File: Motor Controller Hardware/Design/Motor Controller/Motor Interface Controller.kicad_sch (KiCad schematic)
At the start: 0 parts

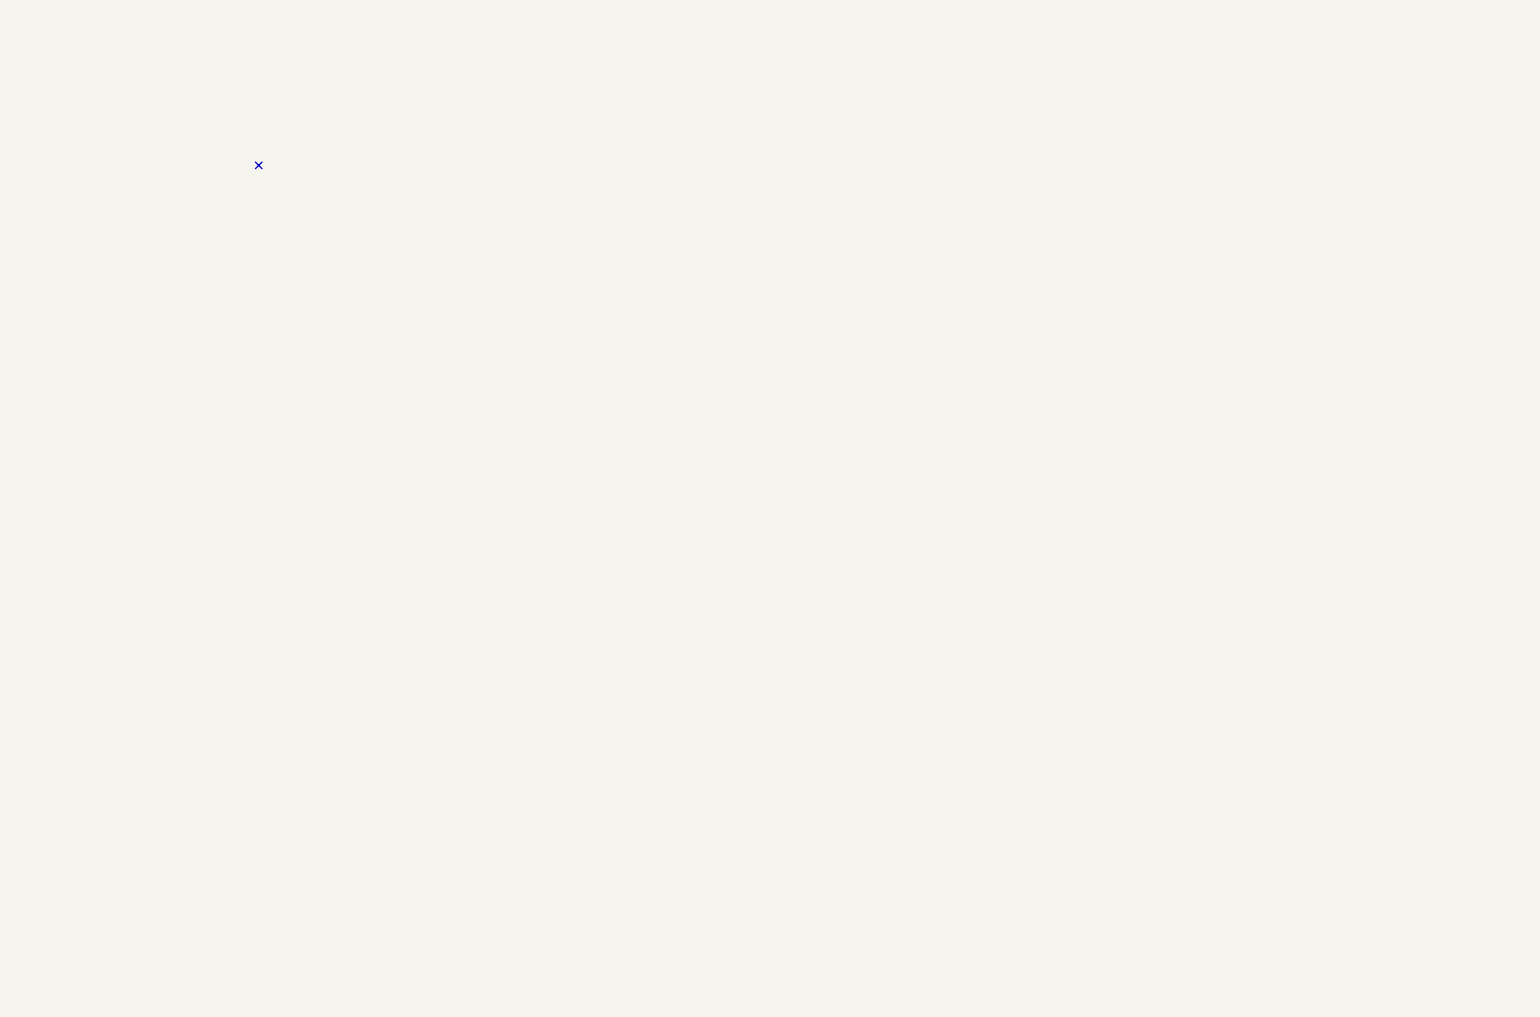
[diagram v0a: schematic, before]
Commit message: Made interface controller and finished gate drive
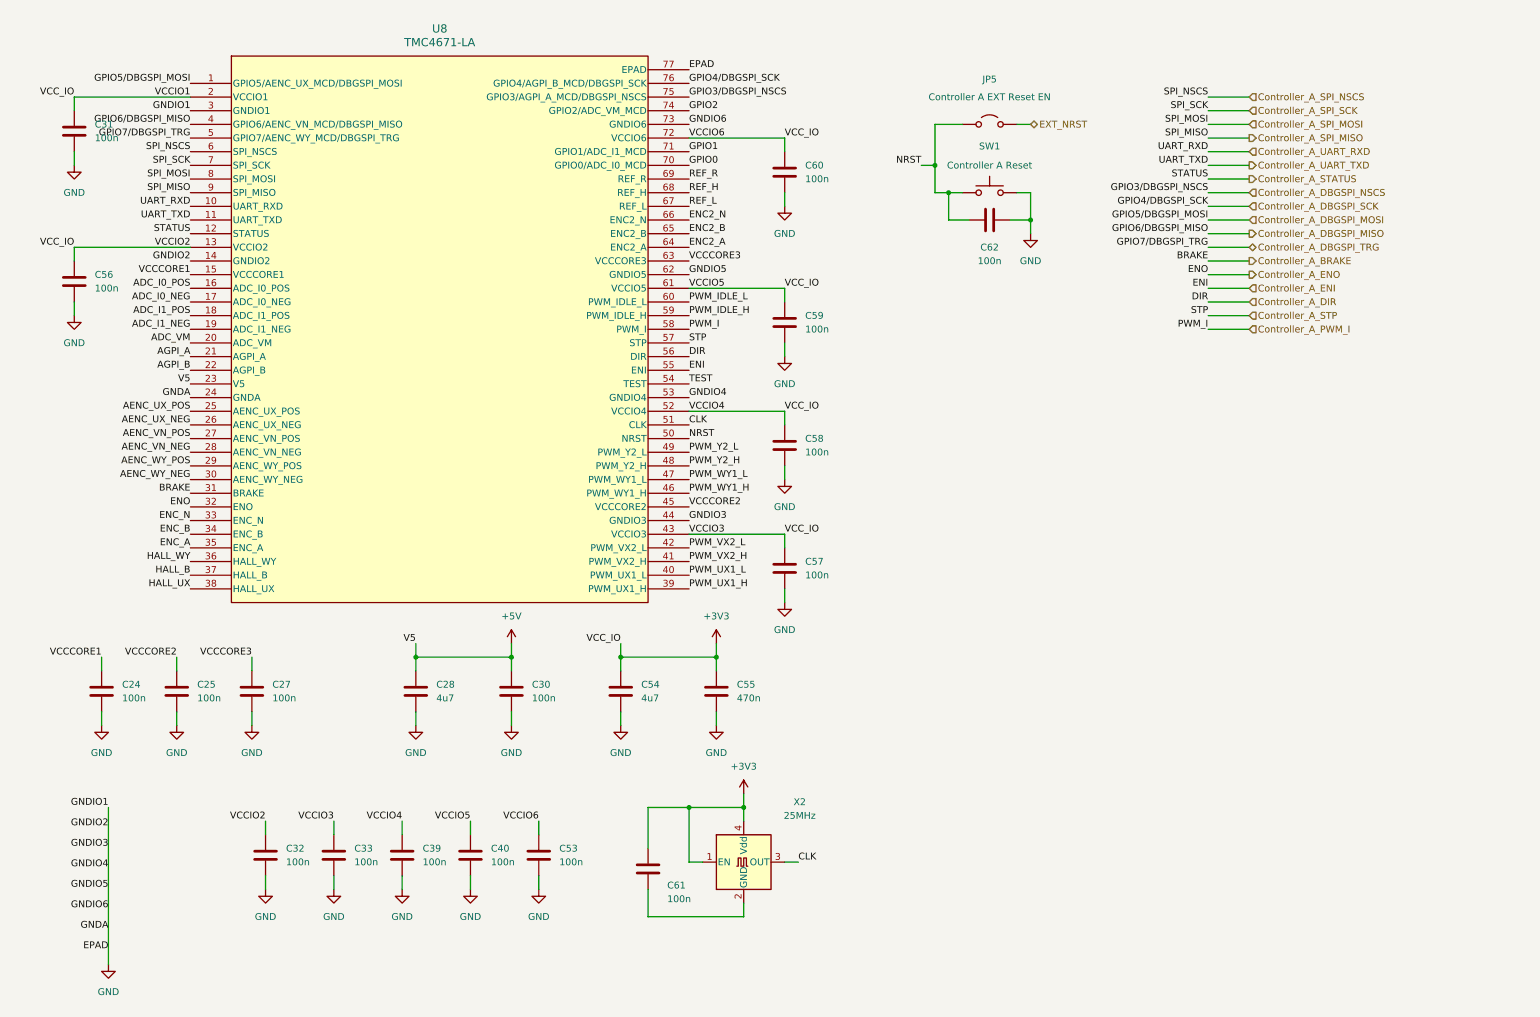
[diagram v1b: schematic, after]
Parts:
- added C24, C25, C27, C30, C31, C32, C33, C39, C40, C53, C56, C57, C58, C59, C60, C61, C62: 100n, symbol Device:C
- added C28, C54: 4u7, symbol Device:C
- added C55: 470n, symbol Device:C
- added JP5: Controller A EXT Reset EN, symbol Jumper:Jumper_2_Open
- added SW1: Controller A Reset, symbol Switch:SW_Push
- added U8: TMC4671-LA, QFN76_10P5X6P5_TRI, symbol Motor Controller:TMC4671-LA
- added X2: 25MHz, Oscillator:Oscillator_SMD_Abracon_ASE-4Pin_3.2x2.5mm, symbol Oscillator:ASE-xxxMHz
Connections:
- new net: C61.2, X2.2 (GND)
- new net +3V3: C31.1, C32.1, C33.1, C39.1, C40.1, C53.1, C54.1, C55.1, C56.1, C57.1, C58.1, C59.1, C60.1, C61.1, U8.13 (VCCIO2), U8.2 (VCCIO1), U8.43 (VCCIO3), U8.52 (VCCIO4), U8.61 (VCCIO5), U8.72 (VCCIO6), X2.1 (EN), X2.4 (Vdd)
- new net +5V: C28.1, C30.1, U8.23 (V5)
- new net ADC_I0_NEG: U8.17 (ADC_I0_NEG)
- new net ADC_I0_POS: U8.16 (ADC_I0_POS)
- new net ADC_I1_NEG: U8.19 (ADC_I1_NEG)
- new net ADC_I1_POS: U8.18 (ADC_I1_POS)
- new net ADC_VM: U8.20 (ADC_VM)
- new net AENC_UX_NEG: U8.26 (AENC_UX_NEG)
- new net AENC_UX_POS: U8.25 (AENC_UX_POS)
- new net AENC_VN_NEG: U8.28 (AENC_VN_NEG)
- new net AENC_VN_POS: U8.27 (AENC_VN_POS)
- new net AENC_WY_NEG: U8.30 (AENC_WY_NEG)
- new net AENC_WY_POS: U8.29 (AENC_WY_POS)
- new net AGPI_A: U8.21 (AGPI_A)
- new net AGPI_B: U8.22 (AGPI_B)
- new net CLK: U8.51 (CLK), X2.3 (OUT)
- new net Controller_A_BRAKE: U8.31 (BRAKE)
- new net Controller_A_DBGSPI_MISO: U8.4 (GPIO6/AENC_VN_MCD/DBGSPI_MISO)
- new net Controller_A_DBGSPI_MOSI: U8.1 (GPIO5/AENC_UX_MCD/DBGSPI_MOSI)
- new net Controller_A_DBGSPI_NSCS: U8.75 (GPIO3/AGPI_A_MCD/DBGSPI_NSCS)
- new net Controller_A_DBGSPI_SCK: U8.76 (GPIO4/AGPI_B_MCD/DBGSPI_SCK)
- new net Controller_A_DBGSPI_TRG: U8.5 (GPIO7/AENC_WY_MCD/DBGSPI_TRG)
- new net Controller_A_DIR: U8.56 (DIR)
- new net Controller_A_ENI: U8.55 (ENI)
- new net Controller_A_ENO: U8.32 (ENO)
- new net Controller_A_PWM_I: U8.58 (PWM_I)
- new net Controller_A_SPI_MISO: U8.9 (SPI_MISO)
- new net Controller_A_SPI_MOSI: U8.8 (SPI_MOSI)
- new net Controller_A_SPI_NSCS: U8.6 (SPI_NSCS)
- new net Controller_A_SPI_SCK: U8.7 (SPI_SCK)
- new net Controller_A_STATUS: U8.12 (STATUS)
- new net Controller_A_STP: U8.57 (STP)
- new net Controller_A_UART_RXD: U8.10 (UART_RXD)
- new net Controller_A_UART_TXD: U8.11 (UART_TXD)
- new net ENC2_A: U8.64 (ENC2_A)
- new net ENC2_B: U8.65 (ENC2_B)
- new net ENC2_N: U8.66 (ENC2_N)
- new net ENC_A: U8.35 (ENC_A)
- new net ENC_B: U8.34 (ENC_B)
- new net ENC_N: U8.33 (ENC_N)
- new net EXT_NRST: JP5.2 (B)
- new net GND: C24.2, C25.2, C27.2, C28.2, C30.2, C31.2, C32.2, C33.2, C39.2, C40.2, C53.2, C54.2, C55.2, C56.2, C57.2, C58.2, C59.2, C60.2, C62.2, SW1.2, U8.14 (GNDIO2), U8.24 (GNDA), U8.3 (GNDIO1), U8.44 (GNDIO3), U8.53 (GNDIO4), U8.62 (GNDIO5), U8.73 (GNDIO6), U8.77 (EPAD)
- new net GPIO0: U8.70 (GPIO0/ADC_I0_MCD)
- new net GPIO1: U8.71 (GPIO1/ADC_I1_MCD)
- new net GPIO2: U8.74 (GPIO2/ADC_VM_MCD)
- new net HALL_B: U8.37 (HALL_B)
- new net HALL_UX: U8.38 (HALL_UX)
- new net HALL_WY: U8.36 (HALL_WY)
- new net NRST: C62.1, JP5.1 (A), SW1.1, U8.50 (NRST)
- new net PWM_IDLE_H: U8.59 (PWM_IDLE_H)
- new net PWM_IDLE_L: U8.60 (PWM_IDLE_L)
- new net PWM_UX1_H: U8.39 (PWM_UX1_H)
- new net PWM_UX1_L: U8.40 (PWM_UX1_L)
- new net PWM_VX2_H: U8.41 (PWM_VX2_H)
- new net PWM_VX2_L: U8.42 (PWM_VX2_L)
- new net PWM_WY1_H: U8.46 (PWM_WY1_H)
- new net PWM_WY1_L: U8.47 (PWM_WY1_L)
- new net PWM_Y2_H: U8.48 (PWM_Y2_H)
- new net PWM_Y2_L: U8.49 (PWM_Y2_L)
- new net REF_H: U8.68 (REF_H)
- new net REF_L: U8.67 (REF_L)
- new net REF_R: U8.69 (REF_R)
- new net TEST: U8.54 (TEST)
- new net VCCCORE1: C24.1, U8.15 (VCCCORE1)
- new net VCCCORE2: C25.1, U8.45 (VCCCORE2)
- new net VCCCORE3: C27.1, U8.63 (VCCCORE3)
- no-connect marks 1 -> 0

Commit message: a:
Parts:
- added C74: 100n, symbol Device:C
- added D8: GREEN, symbol Device:LED
- added FB2: 600R/1A, symbol Device:FerriteBead
- added J15: Controller A NRST, symbol Connector:Screw_Terminal_01x03
- added JP10: Controller A DIR, symbol Jumper:Jumper_2_Open
- added JP13: PWM_H_H, symbol Jumper:Jumper_2_Open
- added JP14: PWM_L_H, symbol Jumper:Jumper_2_Open
- added JP15: PWM_L_L, symbol Jumper:Jumper_2_Open
- added JP16: PWM_H_L, symbol Jumper:Jumper_2_Open
- added JP6: Controller A EXT STATUS, symbol Jumper:Jumper_2_Open
- added JP7: Controller A EXT BRAKE, symbol Jumper:Jumper_2_Open
- added JP8: Controller A ENO, symbol Jumper:Jumper_2_Open
- added JP9: Controller A ENI, symbol Jumper:Jumper_2_Open
- added R10: 11k, symbol Device:R
- added R11: 23k7, symbol Device:R
- added R12, R9: 150k, symbol Device:R
- added R8: 100R, symbol Device:R
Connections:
- net PWM_IDLE_L is gone; now on net PWM_IDLE_H: U8.60 (PWM_IDLE_L)
- net TEST is gone; now on net GND: U8.54 (TEST)
- net +3V3: now also FB2.2, J15.3 (Pin_3), JP13.2 (B), JP14.2 (B); no longer C61.1, X2.1 (EN), X2.4 (Vdd)
- net ADC_VM: now also R10.2, R11.2, R12.1, R9.1
- net Controller_A_BRAKE: now also JP7.2 (B); no longer U8.31 (BRAKE)
- net Controller_A_DIR: now also JP10.2 (B); no longer U8.56 (DIR)
- net Controller_A_ENI: now also JP9.2 (B); no longer U8.55 (ENI)
- net Controller_A_ENO: now also JP8.2 (B); no longer U8.32 (ENO)
- net Controller_A_STATUS: now also JP6.2 (B); no longer U8.12 (STATUS)
- net GND: now also C61.2, X2.2 (GND), C74.2, D8.1 (K), J15.1 (Pin_1), JP15.2 (B), JP16.2 (B), R10.1, R11.1
- net NRST: now also J15.2 (Pin_2)
- net PWM_IDLE_H: now also JP13.1 (A), JP14.1 (A), JP15.1 (A), JP16.1 (A)
- net HALL_B renamed HALL_V
- net PWM_UX1_H renamed Controller_A_UH
- net PWM_UX1_L renamed Controller_A_UL
- net PWM_VX2_H renamed Controller_A_VH
- net PWM_VX2_L renamed Controller_A_VL
- net PWM_WY1_H renamed Controller_A_WH
- net PWM_WY1_L renamed Controller_A_WL
- new net: C61.1, C74.1, FB2.1, X2.1 (EN), X2.4 (Vdd)
- new net: D8.2 (A), R8.1
- new net BRAKE: JP7.1 (A), U8.31 (BRAKE)
- new net DIR: JP10.1 (A), U8.56 (DIR)
- new net ENI: JP9.1 (A), U8.55 (ENI)
- new net ENO: JP8.1 (A), U8.32 (ENO)
- new net STATUS: JP6.1 (A), R8.2, U8.12 (STATUS)
- new net V_{M}: R12.2, R9.2
- no-connect marks 0 -> 2
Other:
- added sheet Controller A Motor Connections (Controller_A_Motor_Connections.kicad_sch)
- note added: "V_{M} is motor nominal voltage, we designed for 48 to 24 volt operation so there is voltage select on these jumpers. Since it is likley there will be mass vibrations these are solder jumpers."
- title: (none) -> HyperDrive Motor Controller
- moved on the sheet: C28, C30, C31, C32, C33, C39, C40, C53, C54, C55, C61, C62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

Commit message: Almost done power delivery
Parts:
- added D24, D25: D_TVS, symbol Device:D_TVS
- added FB5: 600R/1A, symbol Device:FerriteBead
- renumbered C31 to C1, C30 to C10, C40 to C11, C54 to C12, C53 to C13, C61 to C14, C55 to C15, C60 to C16, C59 to C17, C58 to C18, C57 to C19, C56 to C2, C74 to C20, C62 to C21, C24 to C3, C25 to C4, C27 to C5, C32 to C6, C28 to C7, C33 to C8, C39 to C9, D8 to D1, FB2 to FB1, J15 to J7, JP5 to JP1, JP6 to JP10, JP13 to JP2, JP16 to JP3, JP14 to JP4, JP15 to JP5, JP7 to JP6, JP8 to JP7, JP9 to JP8, JP10 to JP9, R8 to R1, R10 to R2, R9 to R3, R11 to R4, R12 to R5, U8 to U1, X2 to X1
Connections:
- net +3V3: now also D25.2 (A2), FB5.2; no longer C1.1, C11.1, C12.1, C13.1, C16.1, C17.1, C18.1, C19.1, C2.1, C6.1, C8.1, C9.1, J7.3 (Pin_3), JP2.2 (B), JP4.2 (B), U1.13 (VCCIO2), U1.2 (VCCIO1), U1.43 (VCCIO3), U1.52 (VCCIO4), U1.61 (VCCIO5), U1.72 (VCCIO6)
- net Controller_A_STP: now also D24.2 (A2), D25.1 (A1)
- net GND: now also D24.1 (A1)
- new net VCCIO1: C1.1, C11.1, C12.1, C13.1, C16.1, C17.1, C18.1, C19.1, C2.1, C6.1, C8.1, C9.1, FB5.1, J7.3 (Pin_3), JP2.2 (B), JP4.2 (B), U1.13 (VCCIO2), U1.2 (VCCIO1), U1.43 (VCCIO3), U1.52 (VCCIO4), U1.61 (VCCIO5), U1.72 (VCCIO6)
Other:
- moved on the sheet: C21, J7, JP1, SW1

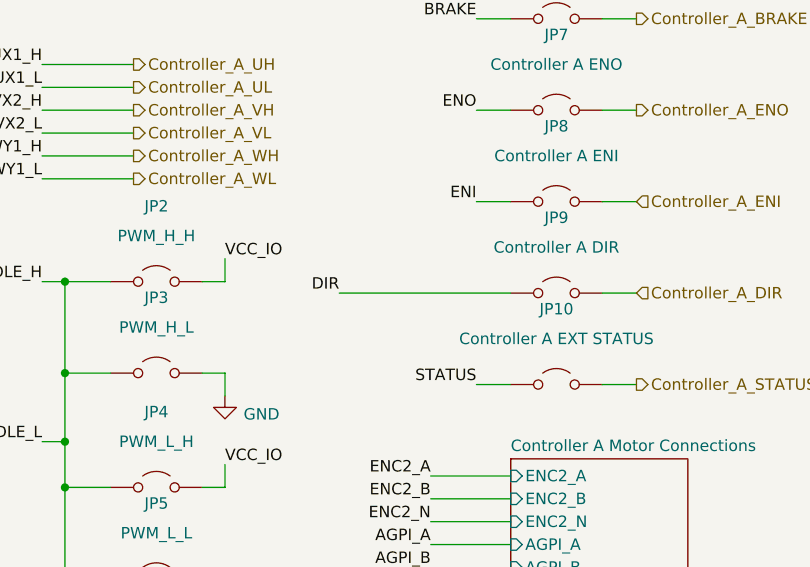
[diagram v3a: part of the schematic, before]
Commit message: Added foot prints and started layout
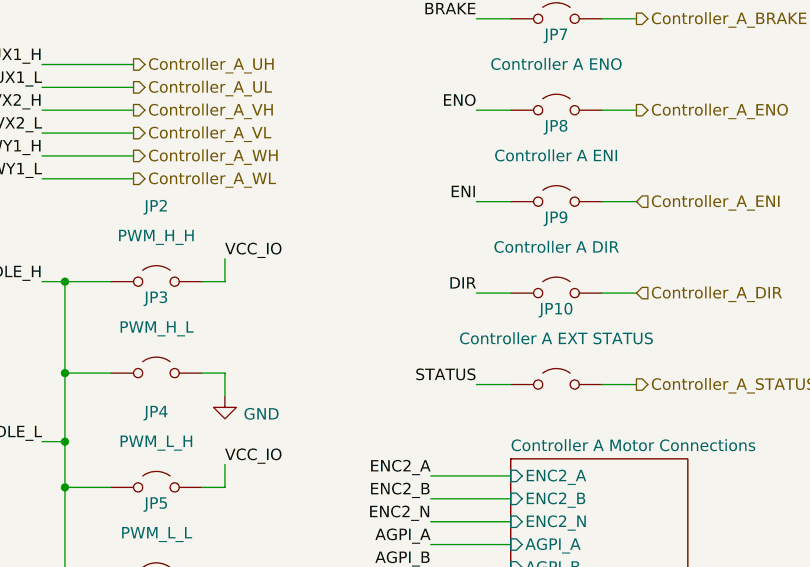
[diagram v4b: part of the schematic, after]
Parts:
- C1, C10, C11, C13, C14, C15, C16, C17, C18, C19, C2, C20, C21, C3, C4, C5, C6, C8, C9: footprint (none) -> Capacitor_SMD:C_0603_1608Metric
- C12, C7: footprint (none) -> Capacitor_SMD:C_0805_2012Metric
- D1: footprint (none) -> LED_SMD:LED_0603_1608Metric
- FB1, FB5: footprint (none) -> Inductor_SMD:L_0805_2012Metric
- J7: footprint (none) -> TerminalBlock_Phoenix:TerminalBlock_Phoenix_MPT-0,5-3-2.54_1x03_P2.54mm_Horizontal
- JP1, JP10, JP2, JP3, JP4, JP5, JP6, JP7, JP8, JP9: footprint (none) -> Connector_PinHeader_2.54mm:PinHeader_1x02_P2.54mm_Vertical
- R1, R2, R3, R4, R5: footprint (none) -> Resistor_SMD:R_0603_1608Metric
- U1: footprint QFN76_10P5X6P5_TRI -> ecocad:QFN76_10P5X6P5_TRI
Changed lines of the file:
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@@
 	(wire
 		(pts
-			(xy 218.44 88.9) (xy 237.49 88.9)
+			(xy 233.68 88.9) (xy 237.49 88.9)
 		)
 		(stroke
@@
 	)
 	(label "DIR"
-		(at 218.44 88.9 180)
+		(at 233.68 88.9 180)
 		(fields_autoplaced yes)
 		(effects
@@
 			)
 		)
-		(property "Footprint" ""
+		(property "Footprint" "Capacitor_SMD:C_0603_1608Metric"
 			(at 122.8852 182.88 0)
 			(effects
@@
 			)
 		)
-		(property "Footprint" ""
+		(property "Footprint" "Inductor_SMD:L_0805_2012Metric"
 			(at 166.37 169.418 90)
 			(effects
@@
 			)
 		)
-		(property "Footprint" ""
+		(property "Footprint" "Capacitor_SMD:C_0603_1608Metric"
 			(at 72.0852 182.88 0)
 			(effects
@@
 			)
 		)
-		(property "Footprint" ""
+		(property "Footprint" "Capacitor_SMD:C_0805_2012Metric"
 			(at 107.6452 142.24 0)
 			(effects
@@
 			)
 		)
-		(property "Footprint" ""
+		(property "Footprint" "Resistor_SMD:R_0603_1608Metric"
 			(at 163.83 136.398 90)
 			(effects
@@
 			)
 		)
-		(property "Footprint" ""
+		(property "Footprint" "Connector_PinHeader_2.54mm:PinHeader_1x02_P2.54mm_Vertical"
 			(at 242.57 58.42 0)
 			(effects
@@
 			)
 		)
-		(property "Footprint" ""
+		(property "Footprint" "Capacitor_SMD:C_0603_1608Metric"
 			(at 84.7852 182.88 0)
 			(effects
@@
 			)
 		)
-		(property "Footprint" ""
+		(property "Footprint" "Resistor_SMD:R_0603_1608Metric"
 			(at 159.258 140.97 90)
 			(effects
@@
 			)
 		)
-		(property "Footprint" ""
+		(property "Footprint" "LED_SMD:LED_0603_1608Metric"
 			(at 40.64 179.07 0)
 			(effects
@@
 			)
 		)
-		(property "Footprint" ""
+		(property "Footprint" "Capacitor_SMD:C_0603_1608Metric"
 			(at 21.2852 38.1 0)
 			(effects
@@
 			)
 		)
-		(property "Footprint" ""
+		(property "Footprint" "Connector_PinHeader_2.54mm:PinHeader_1x02_P2.54mm_Vertical"
 			(at 242.57 88.9 0)
 			(effects
@@
 			)
 		)
-		(property "Footprint" ""
+		(property "Footprint" "Capacitor_SMD:C_0603_1608Metric"
 			(at 59.3852 182.88 0)
 			(effects
@@
 			)
 		)
-		(property "Footprint" ""
+		(property "Footprint" "Capacitor_SMD:C_0603_1608Metric"
 			(at 158.4452 180.34 0)
 			(effects
@@
 			)
 		)
-		(property "Footprint" ""
+		(property "Footprint" "Capacitor_SMD:C_0603_1608Metric"
 			(at 87.3252 142.24 0)
 			(effects
@@
 			)
 		)
-		(property "Footprint" ""
+		(property "Footprint" "Connector_PinHeader_2.54mm:PinHeader_1x02_P2.54mm_Vertical"
 			(at 198.12 87.63 0)
 			(effects
@@
 			)
 		)
-		(property "Footprint" ""
+		(property "Footprint" "Capacitor_SMD:C_0603_1608Metric"
 			(at 125.4252 142.24 0)
 			(effects
@@
 			)
 		)
-		(property "Footprint" ""
+		(property "Footprint" "Capacitor_SMD:C_0603_1608Metric"
 			(at 155.9052 73.66 0)
 			(effects
@@
 			)
 		)
-		(property "Footprint" ""
+		(property "Footprint" "Connector_PinHeader_2.54mm:PinHeader_1x02_P2.54mm_Vertical"
 			(at 198.12 97.79 0)
 			(effects
@@
 			)
 		)
-		(property "Footprint" ""
+		(property "Footprint" "Connector_PinHeader_2.54mm:PinHeader_1x02_P2.54mm_Vertical"
 			(at 242.57 99.06 0)
 			(effects
@@
 			)
 		)
-		(property "Footprint" ""
+		(property "Footprint" "Capacitor_SMD:C_0603_1608Metric"
 			(at 155.9052 96.52 0)
 			(effects
@@
 			)
 		)
-		(property "Footprint" ""
+		(property "Footprint" "Capacitor_SMD:C_0603_1608Metric"
 			(at 56.8452 142.24 0)
 			(effects
@@
 			)
 		)
-		(property "Footprint" ""
+		(property "Footprint" "Capacitor_SMD:C_0805_2012Metric"
 			(at 69.5452 142.24 0)
 			(effects
@@
 			)
 		)
-		(property "Footprint" "QFN76_10P5X6P5_TRI"
+		(property "Footprint" "ecocad:QFN76_10P5X6P5_TRI"
 			(at 89.916 7.366 0)
 			(effects
@@
 			)
 		)
-		(property "Footprint" ""
+		(property "Footprint" "Capacitor_SMD:C_0603_1608Metric"
 			(at 155.9052 119.38 0)
 			(effects
@@
 			)
 		)
-		(property "Footprint" ""
+		(property "Footprint" "Capacitor_SMD:C_0603_1608Metric"
 			(at 155.9052 45.72 0)
 			(effects
@@
 			)
 		)
-		(property "Footprint" ""
+		(property "Footprint" "Connector_PinHeader_2.54mm:PinHeader_1x02_P2.54mm_Vertical"
 			(at 198.12 120.65 0)
 			(effects
@@
 			)
 		)
-		(property "Footprint" ""
+		(property "Footprint" "Resistor_SMD:R_0603_1608Metric"
 			(at 196.85 136.398 90)
 			(effects
@@
 			)
 		)
-		(property "Footprint" ""
+		(property "Footprint" "Resistor_SMD:R_0603_1608Metric"
 			(at 192.278 140.97 90)
 			(effects
@@
 			)
 		)
-		(property "Footprint" ""
+		(property "Footprint" "Capacitor_SMD:C_0603_1608Metric"
 			(at 23.8252 66.04 0)
 			(effects
@@
 			)
 		)
-		(property "Footprint" ""
+		(property "Footprint" "Inductor_SMD:L_0805_2012Metric"
 			(at 115.57 133.858 90)
 			(effects
@@
 			)
 		)
-		(property "Footprint" ""
+		(property "Footprint" "Resistor_SMD:R_0603_1608Metric"
 			(at 42.418 168.91 90)
 			(effects
@@
 			)
 		)
-		(property "Footprint" ""
+		(property "Footprint" "Connector_PinHeader_2.54mm:PinHeader_1x02_P2.54mm_Vertical"
 			(at 181.61 21.59 0)
 			(effects
@@
 			)
 		)
-		(property "Footprint" ""
+		(property "Footprint" "Connector_PinHeader_2.54mm:PinHeader_1x02_P2.54mm_Vertical"
 			(at 242.57 68.58 0)
 			(effects
@@
 			)
 		)
-		(property "Footprint" ""
+		(property "Footprint" "Capacitor_SMD:C_0603_1608Metric"
 			(at 42.8752 142.24 0)
 			(effects
@@
 			)
 		)
-		(property "Footprint" ""
+		(property "Footprint" "Capacitor_SMD:C_0603_1608Metric"
 			(at 97.4852 182.88 0)
 			(effects
@@
 			)
 		)
-		(property "Footprint" ""
+		(property "Footprint" "TerminalBlock_Phoenix:TerminalBlock_Phoenix_MPT-0,5-3-2.54_1x03_P2.54mm_Horizontal"
 			(at 200.66 52.07 0)
 			(effects
@@
 			)
 		)
-		(property "Footprint" ""
+		(property "Footprint" "Connector_PinHeader_2.54mm:PinHeader_1x02_P2.54mm_Vertical"
 			(at 242.57 78.74 0)
 			(effects
@@
 			)
 		)
-		(property "Footprint" ""
+		(property "Footprint" "Capacitor_SMD:C_0603_1608Metric"
 			(at 28.9052 142.24 0)
 			(effects
@@
 			)
 		)
-		(property "Footprint" ""
+		(property "Footprint" "Connector_PinHeader_2.54mm:PinHeader_1x02_P2.54mm_Vertical"
 			(at 198.12 110.49 0)
 			(effects
@@
 			)
 		)
-		(property "Footprint" ""
+		(property "Footprint" "Capacitor_SMD:C_0603_1608Metric"
 			(at 185.42 38.4048 0)
 			(effects
@@
 			)
 		)
-		(property "Footprint" ""
+		(property "Footprint" "Capacitor_SMD:C_0603_1608Metric"
 			(at 110.1852 182.88 0)
 			(effects
